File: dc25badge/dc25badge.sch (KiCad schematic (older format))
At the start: 34 parts, among them P1 BATT, P2 USB_OTG, P3 CORTEX, Q1 DMN1019USN, SW1 RESET, SW3 MODE, SW4 BRIGHT, U1 MIC5305, U2 TPS61232, U3 ATSAMD21E18A-AU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

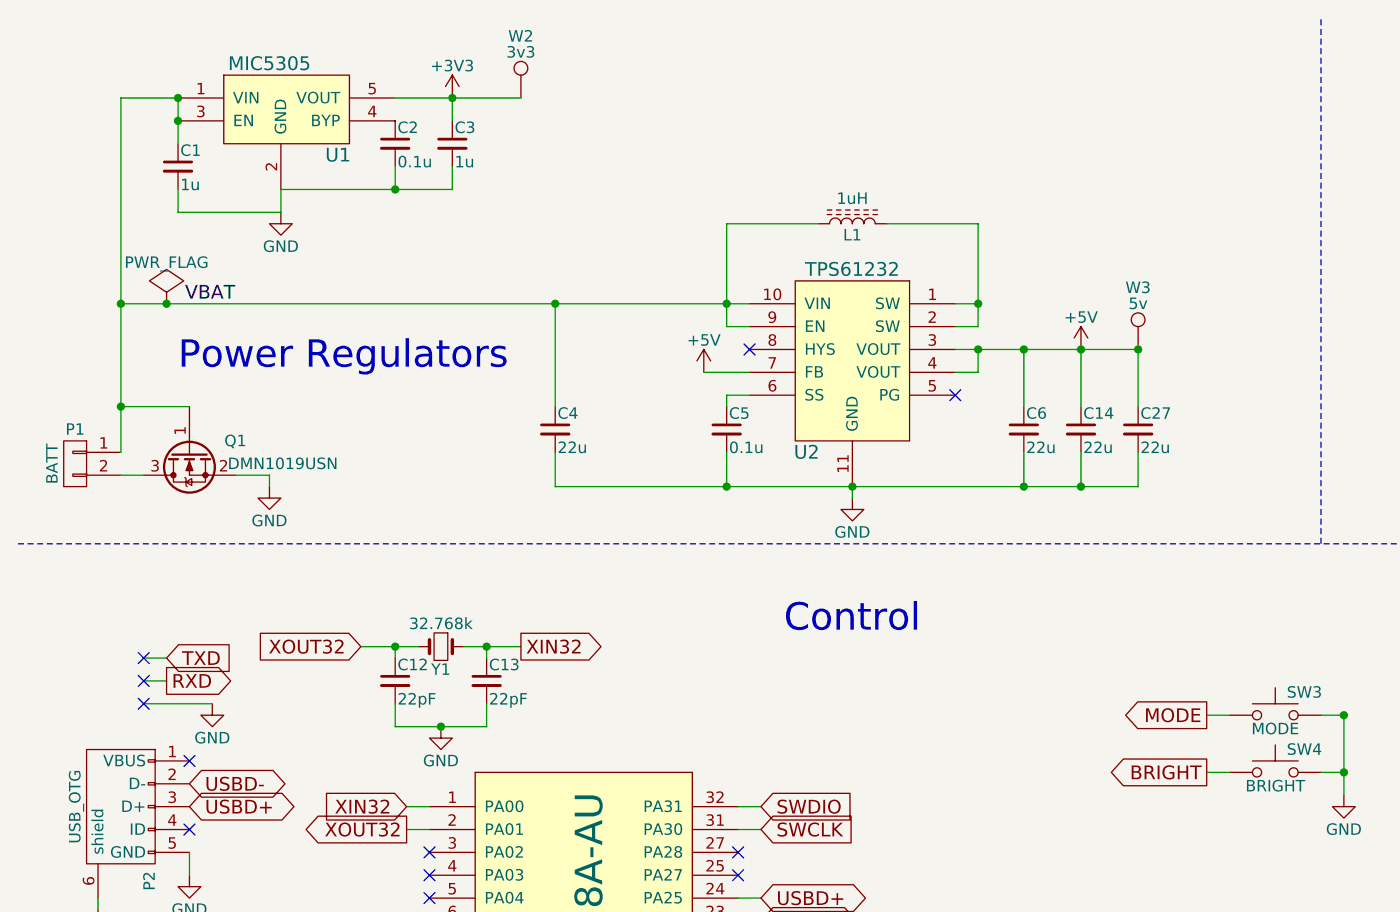
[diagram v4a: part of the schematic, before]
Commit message: More cap for noise.
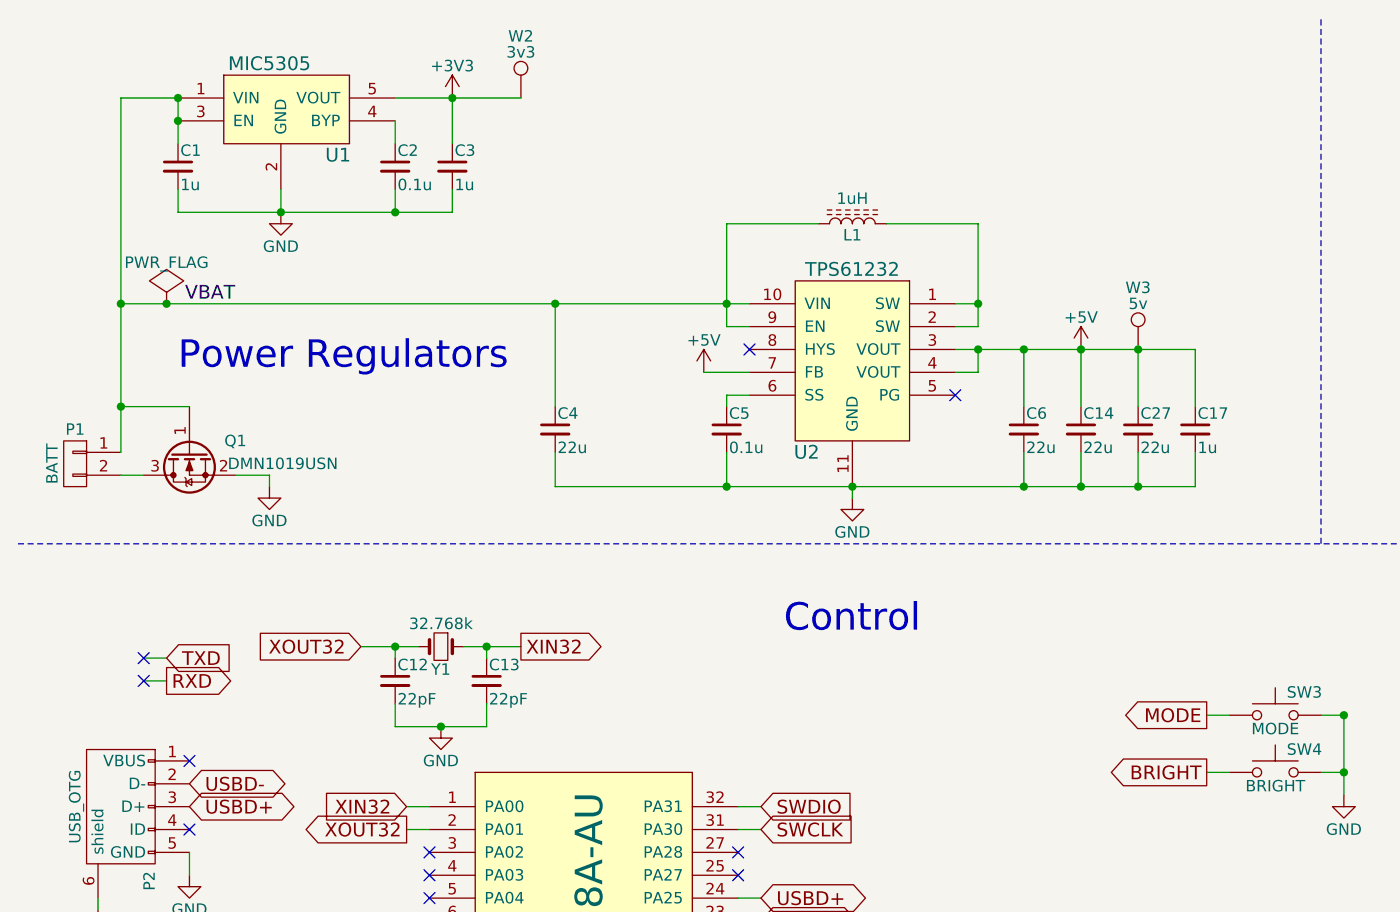
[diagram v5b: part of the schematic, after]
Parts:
- added C17: 1u, Capacitors_SMD:C_0805, symbol C_Small
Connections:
- net +5V: now also C17.1
- net GND: now also C17.2
- no-connect marks 26 -> 25
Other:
- moved on the sheet: C2, C3
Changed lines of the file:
@@
 $EndDescr
 $Comp
-L +5V #PWR01
+L +5V #PWR20
 U 1 1 592A4C04
 P 5150 1950
-F 0 "#PWR01" H 5150 1800 50  0001 C CNN
+F 0 "#PWR20" H 5150 1800 50  0001 C CNN
 F 1 "+5V" H 5150 2090 50  0000 C CNN
 F 2 "" H 5150 1950 50  0000 C CNN
@@
 L C_Small C2
 U 1 1 592A53A0
-P 2150 1050
-F 0 "C2" H 2160 1120 50  0000 L CNN
-F 1 "0.1u" H 2160 970 50  0000 L CNN
-F 2 "Capacitors_SMD:C_0805" H 2150 1050 50  0001 C CNN
-F 3 "" H 2150 1050 50  0000 C CNN
-	1    2150 1050
+P 2150 1150
+F 0 "C2" H 2160 1220 50  0000 L CNN
+F 1 "0.1u" H 2160 1070 50  0000 L CNN
+F 2 "Capacitors_SMD:C_0805" H 2150 1150 50  0001 C CNN
+F 3 "" H 2150 1150 50  0000 C CNN
+	1    2150 1150
 	1    0    0    -1
 $EndComp
@@
 L C_Small C3
 U 1 1 592A543D
-P 2400 1050
-F 0 "C3" H 2410 1120 50  0000 L CNN
-F 1 "1u" H 2410 970 50  0000 L CNN
-F 2 "Capacitors_SMD:C_0805" H 2400 1050 50  0001 C CNN
-F 3 "" H 2400 1050 50  0000 C CNN
-	1    2400 1050
-	1    0    0    -1
-$EndComp
-$Comp
-L GND #PWR02
+P 2400 1150
+F 0 "C3" H 2410 1220 50  0000 L CNN
+F 1 "1u" H 2410 1070 50  0000 L CNN
+F 2 "Capacitors_SMD:C_0805" H 2400 1150 50  0001 C CNN
+F 3 "" H 2400 1150 50  0000 C CNN
+	1    2400 1150
+	1    0    0    -1
+$EndComp
+$Comp
+L GND #PWR6
 U 1 1 592A5659
 P 1600 2550
-F 0 "#PWR02" H 1600 2300 50  0001 C CNN
+F 0 "#PWR6" H 1600 2300 50  0001 C CNN
 F 1 "GND" H 1600 2400 50  0000 C CNN
 F 2 "" H 1600 2550 50  0000 C CNN
@@
 $EndComp
 $Comp
-L GND #PWR03
+L GND #PWR7
 U 1 1 592A568F
 P 1650 1350
-F 0 "#PWR03" H 1650 1100 50  0001 C CNN
+F 0 "#PWR7" H 1650 1100 50  0001 C CNN
 F 1 "GND" H 1650 1200 50  0000 C CNN
 F 2 "" H 1650 1350 50  0000 C CNN
@@
 $EndComp
 $Comp
-L +3V3 #PWR04
+L +3V3 #PWR12
 U 1 1 592A5759
 P 2400 850
-F 0 "#PWR04" H 2400 700 50  0001 C CNN
+F 0 "#PWR12" H 2400 700 50  0001 C CNN
 F 1 "+3V3" H 2400 990 50  0000 C CNN
 F 2 "" H 2400 850 50  0000 C CNN
@@
 $EndComp
 $Comp
-L GND #PWR05
+L GND #PWR10
 U 1 1 592A794C
 P 2200 5650
-F 0 "#PWR05" H 2200 5400 50  0001 C CNN
+F 0 "#PWR10" H 2200 5400 50  0001 C CNN
 F 1 "GND" H 2200 5500 50  0000 C CNN
 F 2 "" H 2200 5650 50  0000 C CNN
@@
 $EndComp
 $Comp
-L +3V3 #PWR06
+L +3V3 #PWR4
 U 1 1 592A7D9A
 P 1400 4900
-F 0 "#PWR06" H 1400 4750 50  0001 C CNN
+F 0 "#PWR4" H 1400 4750 50  0001 C CNN
 F 1 "+3V3" H 1400 5040 50  0000 C CNN
 F 2 "" H 1400 4900 50  0000 C CNN
@@
 $EndComp
 $Comp
-L GND #PWR07
+L GND #PWR5
 U 1 1 592A7E37
 P 1400 5800
-F 0 "#PWR07" H 1400 5550 50  0001 C CNN
+F 0 "#PWR5" H 1400 5550 50  0001 C CNN
 F 1 "GND" H 1400 5650 50  0000 C CNN
 F 2 "" H 1400 5800 50  0000 C CNN
@@
 $EndComp
 $Comp
-L GND #PWR08
+L GND #PWR16
 U 1 1 592A8194
 P 3750 5750
-F 0 "#PWR08" H 3750 5500 50  0001 C CNN
+F 0 "#PWR16" H 3750 5500 50  0001 C CNN
 F 1 "GND" H 3750 5600 50  0000 C CNN
 F 2 "" H 3750 5750 50  0000 C CNN
@@
 $EndComp
 $Comp
-L +3V3 #PWR09
+L +3V3 #PWR18
 U 1 1 592A8397
 P 4200 5100
-F 0 "#PWR09" H 4200 4950 50  0001 C CNN
+F 0 "#PWR18" H 4200 4950 50  0001 C CNN
 F 1 "+3V3" H 4200 5240 50  0000 C CNN
 F 2 "" H 4200 5100 50  0000 C CNN
@@
 ~RESET
 $Comp
-L +3V3 #PWR010
+L +3V3 #PWR8
 U 1 1 592A8A6B
 P 1650 6150
-F 0 "#PWR010" H 1650 6000 50  0001 C CNN
+F 0 "#PWR8" H 1650 6000 50  0001 C CNN
 F 1 "+3V3" H 1650 6290 50  0000 C CNN
 F 2 "" H 1650 6150 50  0000 C CNN
@@
 $EndComp
 $Comp
-L GND #PWR011
+L GND #PWR9
 U 1 1 592A9161
 P 1650 7000
-F 0 "#PWR011" H 1650 6750 50  0001 C CNN
+F 0 "#PWR9" H 1650 6750 50  0001 C CNN
 F 1 "GND" H 1650 6850 50  0000 C CNN
 F 2 "" H 1650 7000 50  0000 C CNN
@@
 NoConn ~ 3250 6800
 $Comp
-L GND #PWR012
+L GND #PWR14
 U 1 1 592A986B
 P 2550 6950
-F 0 "#PWR012" H 2550 6700 50  0001 C CNN
+F 0 "#PWR14" H 2550 6700 50  0001 C CNN
 F 1 "GND" H 2550 6800 50  0000 C CNN
 F 2 "" H 2550 6950 50  0000 C CNN
@@
 $EndComp
 $Comp
-L +3V3 #PWR013
+L +3V3 #PWR13
 U 1 1 592A99A6
 P 2550 6500
-F 0 "#PWR013" H 2550 6350 50  0001 C CNN
+F 0 "#PWR13" H 2550 6350 50  0001 C CNN
 F 1 "+3V3" H 2550 6640 50  0000 C CNN
 F 2 "" H 2550 6500 50  0000 C CNN
@@
 $EndComp
 $Comp
-L GND #PWR014
+L GND #PWR2
 U 1 1 592AA720
 P 1250 4250
-F 0 "#PWR014" H 1250 4000 50  0001 C CNN
+F 0 "#PWR2" H 1250 4000 50  0001 C CNN
 F 1 "GND" H 1250 4100 50  0000 C CNN
 F 2 "" H 1250 4250 50  0000 C CNN
@@
 SPI_MOSI
 Wire Wire Line
-	2400 1250 2400 1150
-Wire Wire Line
-	1650 1250 2400 1250
-Wire Wire Line
-	2150 1150 2150 1250
-Connection ~ 2150 1250
+	2400 1350 2400 1250
+Wire Wire Line
+	1200 1350 2400 1350
 Wire Wire Line
 	1200 850  1200 1050
@@
 	1200 1250 1200 1350
 Wire Wire Line
-	1200 1350 1650 1350
-Wire Wire Line
 	1650 1350 1650 1250
 Wire Wire Line
-	2400 950  2400 850
+	2400 850  2400 1050
 Wire Wire Line
 	2150 850  2700 850
@@
 $EndComp
 $Comp
-L PWR_FLAG #FLG016
+L PWR_FLAG #FLG1
 U 1 1 592AD95C
 P 1150 1750
-F 0 "#FLG016" H 1150 1845 50  0001 C CNN
+F 0 "#FLG1" H 1150 1845 50  0001 C CNN
 F 1 "PWR_FLAG" H 1150 1930 50  0000 C CNN
 F 2 "" H 1150 1750 50  0000 C CNN
@@
 	4700 6700 4700 6800
 $Comp
-L +5V #PWR017
+L +5V #PWR21
 U 1 1 592AE3BE
 P 5250 6750
-F 0 "#PWR017" H 5250 6600 50  0001 C CNN
+F 0 "#PWR21" H 5250 6600 50  0001 C CNN
 F 1 "+5V" H 5250 6890 50  0000 C CNN
 F 2 "" H 5250 6750 50  0000 C CNN
@@
 	4250 6400 4250 7200
 $Comp
-L GND #PWR018
+L GND #PWR19
 U 1 1 592AE5B3
 P 4250 7200
-F 0 "#PWR018" H 4250 6950 50  0001 C CNN
+F 0 "#PWR19" H 4250 6950 50  0001 C CNN
 F 1 "GND" H 4250 7050 50  0000 C CNN
 F 2 "" H 4250 7200 50  0000 C CNN
@@
 	2300 4850 2200 4850
 NoConn ~ 3650 4550
-$Comp
-L GND #PWR019
-U 1 1 592B0060
-P 1350 3500
-F 0 "#PWR019" H 1350 3250 50  0001 C CNN
-F 1 "GND" H 1350 3350 50  0000 C CNN
-F 2 "" H 1350 3500 50  0000 C CNN
-F 3 "" H 1350 3500 50  0000 C CNN
-	1    1350 3500
-	1    0    0    -1
-$EndComp
-Wire Wire Line
-	1050 3500 1350 3500
 Text GLabel 1150 3300 2    60   Input ~ 0
 TXD
@@
 Connection ~ 2150 3250
 $Comp
-L GND #PWR020
+L GND #PWR11
 U 1 1 592B1083
 P 2350 3600
-F 0 "#PWR020" H 2350 3350 50  0001 C CNN
+F 0 "#PWR11" H 2350 3350 50  0001 C CNN
 F 1 "GND" H 2350 3450 50  0000 C CNN
 F 2 "" H 2350 3600 50  0000 C CNN
@@
 	5700 3550 5800 3550
 $Comp
-L GND #PWR021
+L GND #PWR22
 U 1 1 592BA362
 P 6300 3900
-F 0 "#PWR021" H 6300 3650 50  0001 C CNN
+F 0 "#PWR22" H 6300 3650 50  0001 C CNN
 F 1 "GND" H 6300 3750 50  0000 C CNN
 F 2 "" H 6300 3900 50  0000 C CNN
@@
 $EndComp
 $Comp
-L GND #PWR022
+L GND #PWR17
 U 1 1 592C536E
 P 4150 2600
-F 0 "#PWR022" H 4150 2350 50  0001 C CNN
+F 0 "#PWR17" H 4150 2350 50  0001 C CNN
 F 1 "GND" H 4150 2450 50  0000 C CNN
 F 2 "" H 4150 2600 50  0000 C CNN
@@
 Connection ~ 4150 2550
 Wire Wire Line
-	2850 2550 5400 2550
+	2850 2550 5650 2550
 Wire Wire Line
 	3600 2550 3600 2400
@@
 NoConn ~ 3700 1950
 $Comp
-L +5V #PWR023
+L +5V #PWR15
 U 1 1 592C61C0
 P 3500 2050
-F 0 "#PWR023" H 3500 1900 50  0001 C CNN
+F 0 "#PWR15" H 3500 1900 50  0001 C CNN
 F 1 "+5V" H 3500 2190 50  0000 C CNN
 F 2 "" H 3500 2050 50  0000 C CNN
@@
 Connection ~ 4900 2550
 Wire Wire Line
-	4600 1950 5400 1950
+	4600 1950 5650 1950
 Wire Wire Line
 	5400 1950 5400 2200
@@
 Wire Wire Line
 	2300 4650 2200 4650
-NoConn ~ 1050 3500
 NoConn ~ 1050 3400
 NoConn ~ 1050 3300
 $Comp
-L GND #PWR024
+L GND #PWR1
 U 1 1 592CB85E
 P 850 4400
-F 0 "#PWR024" H 850 4150 50  0001 C CNN
+F 0 "#PWR1" H 850 4150 50  0001 C CNN
 F 1 "GND" H 850 4250 50  0000 C CNN
 F 2 "" H 850 4400 50  0000 C CNN
@@
 $EndComp
 $Comp
-L GND #PWR025
+L GND #PWR23
 U 1 1 59345803
 P 6750 4900
-F 0 "#PWR025" H 6750 4650 50  0001 C CNN
+F 0 "#PWR23" H 6750 4650 50  0001 C CNN
 F 1 "GND" H 6750 4750 50  0000 C CNN
 F 2 "" H 6750 4900 50  0000 C CNN
@@
 $EndComp
 $Comp
-L GND #PWR026
+L GND #PWR24
 U 1 1 5934585D
 P 6750 5600
-F 0 "#PWR026" H 6750 5350 50  0001 C CNN
+F 0 "#PWR24" H 6750 5350 50  0001 C CNN
 F 1 "GND" H 6750 5450 50  0000 C CNN
 F 2 "" H 6750 5600 50  0000 C CNN
@@
 $EndComp
 $Comp
-L GND #PWR027
+L GND #PWR25
 U 1 1 59347BAA
 P 6850 6250
-F 0 "#PWR027" H 6850 6000 50  0001 C CNN
+F 0 "#PWR25" H 6850 6000 50  0001 C CNN
 F 1 "GND" H 6850 6100 50  0000 C CNN
 F 2 "" H 6850 6250 50  0000 C CNN
@@
 	1250 2200 950  2200
 Connection ~ 950  2200
+Wire Wire Line
+	2150 1250 2150 1350
+Connection ~ 2150 1350
+Wire Wire Line
+	2150 1050 2150 950
+Connection ~ 1650 1350
+$Comp
+L C_Small C17
+U 1 1 593A4319
+P 5650 2300
+F 0 "C17" H 5660 2370 50  0000 L CNN
+F 1 "1u" H 5660 2220 50  0000 L CNN
+F 2 "Capacitors_SMD:C_0805" H 5650 2300 50  0001 C CNN
+F 3 "" H 5650 2300 50  0000 C CNN
+	1    5650 2300
+	1    0    0    -1
+$EndComp
+Wire Wire Line
+	5650 2550 5650 2400
+Connection ~ 5400 2550
+Wire Wire Line
+	5650 1950 5650 2200
 $EndSCHEMATC
